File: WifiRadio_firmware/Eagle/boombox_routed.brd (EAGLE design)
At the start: 60.6 x 45.7 mm, 16 parts, among them Y1 16 MHz

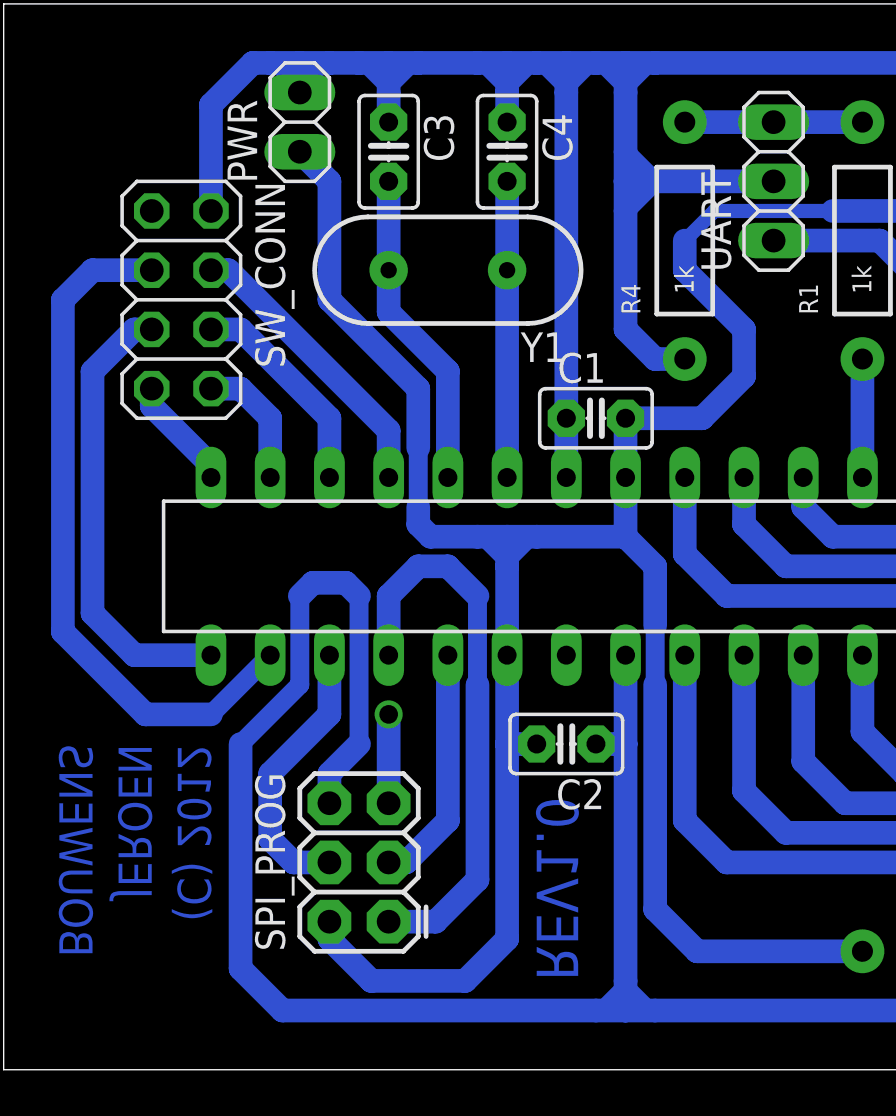
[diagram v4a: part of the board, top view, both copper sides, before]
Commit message: More angle changes
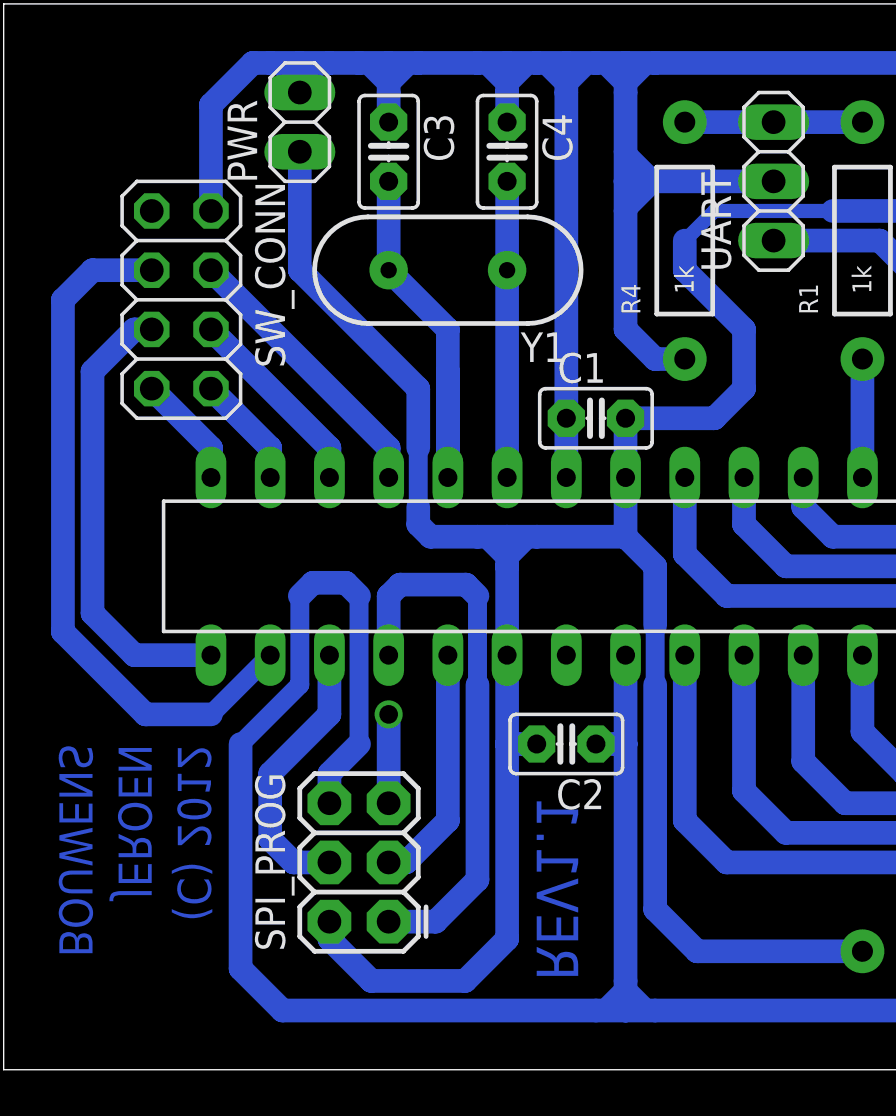
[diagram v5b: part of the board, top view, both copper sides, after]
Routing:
- net N$1: track 13.8 -> 18.3 mm
- net N$23: track 5.61 -> 4.86 mm
- net N$22: track 9.20 -> 8.45 mm
- net N$17: track 24.1 -> 23.5 mm
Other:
- board text added: "REV1.1"
- board text removed: "REV1.0"
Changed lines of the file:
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@@
 <layer number="23" name="tOrigins" color="15" fill="1" visible="yes" active="yes"/>
 <layer number="24" name="bOrigins" color="15" fill="1" visible="yes" active="yes"/>
-<layer number="25" name="tNames" color="7" fill="1" visible="no" active="yes"/>
-<layer number="26" name="bNames" color="7" fill="1" visible="no" active="yes"/>
+<layer number="25" name="tNames" color="7" fill="1" visible="yes" active="yes"/>
+<layer number="26" name="bNames" color="7" fill="1" visible="yes" active="yes"/>
 <layer number="27" name="tValues" color="7" fill="1" visible="no" active="yes"/>
 <layer number="28" name="bValues" color="7" fill="1" visible="no" active="yes"/>
@@
 <text x="8.89" y="15.24" size="1.4224" layer="16" ratio="25" rot="MR270">JEROEN</text>
 <text x="6.35" y="15.24" size="1.4224" layer="16" ratio="25" rot="MR270">BOUWENS</text>
-<text x="25.4" y="5.08" size="1.778" layer="16" ratio="23" rot="MR90">REV1.0</text>
+<text x="25.4" y="5.08" size="1.778" layer="16" ratio="23" rot="MR90">REV1.1</text>
 </plain>
 <attributes>
@@
 <wire x1="24.13" y1="6.87605" x2="22.33395" y2="5.08" width="1.016" layer="16"/>
 <wire x1="22.33395" y1="5.08" x2="18.30605" y2="5.08" width="1.016" layer="16"/>
-<wire x1="31.75" y1="36.83" x2="31.75" y2="35.56" width="1.016" layer="16"/>
-<wire x1="31.75" y1="35.56" x2="34.29" y2="33.02" width="1.016" layer="16"/>
-<wire x1="34.29" y1="33.02" x2="34.29" y2="31.00605" width="1.016" layer="16"/>
-<wire x1="34.29" y1="31.00605" x2="32.49395" y2="29.21" width="1.016" layer="16"/>
-<wire x1="32.49395" y1="29.21" x2="29.21" y2="29.21" width="1.016" layer="16"/>
 <wire x1="48.26" y1="35.56" x2="43.92395" y2="35.56" width="1.016" layer="16"/>
 <wire x1="43.92395" y1="35.56" x2="41.38395" y2="38.1" width="1.016" layer="16"/>
@@
 <wire x1="20.84605" y1="24.13" x2="20.32" y2="24.65605" width="1.016" layer="16"/>
 <wire x1="20.32" y1="24.65605" x2="20.32" y2="25.4" width="1.016" layer="16"/>
-<wire x1="15.24" y1="40.64" x2="16.51" y2="39.37" width="1.016" layer="16"/>
-<wire x1="16.51" y1="39.37" x2="16.51" y2="34.29" width="1.016" layer="16"/>
+<wire x1="15.24" y1="40.64" x2="15.24" y2="35.56" width="1.016" layer="16"/>
 <wire x1="20.32" y1="27.94" x2="20.32" y2="25.4" width="0.8128" layer="16"/>
 <wire x1="24.13" y1="19.05" x2="24.13" y2="22.86" width="1.016" layer="16"/>
@@
 <wire x1="32.27605" y1="6.35" x2="30.48" y2="8.14605" width="1.016" layer="16"/>
 <wire x1="30.48" y1="8.14605" x2="30.48" y2="17.78" width="1.016" layer="16"/>
-<wire x1="16.51" y1="34.29" x2="20.32" y2="30.48" width="1.016" layer="16"/>
+<wire x1="15.24" y1="35.56" x2="20.32" y2="30.48" width="1.016" layer="16"/>
 <wire x1="20.32" y1="30.48" x2="20.32" y2="27.94" width="1.016" layer="16"/>
 <wire x1="24.13" y1="22.86" x2="25.4" y2="24.13" width="0.4064" layer="16"/>
@@
 <wire x1="58.42" y1="35.56" x2="59.69" y2="34.29" width="1.016" layer="16"/>
 <wire x1="59.69" y1="34.29" x2="59.69" y2="36.83" width="1.016" layer="16"/>
-<wire x1="46.99" y1="19.05" x2="46.99" y2="17.78" width="0" layer="19" extent="16-16"/>
 <wire x1="46.99" y1="19.05" x2="46.99" y2="17.78" width="1.016" layer="16"/>
+<wire x1="29.21" y1="29.21" x2="33.02" y2="29.21" width="1.016" layer="16"/>
+<wire x1="33.02" y1="29.21" x2="34.29" y2="30.48" width="1.016" layer="16"/>
+<wire x1="34.29" y1="30.48" x2="34.29" y2="33.02" width="1.016" layer="16"/>
+<wire x1="34.29" y1="33.02" x2="31.75" y2="35.56" width="1.016" layer="16"/>
+<wire x1="31.75" y1="35.56" x2="31.75" y2="36.83" width="1.016" layer="16"/>
 </signal>
 <signal name="GND">
@@
 <contactref element="C3" pad="2"/>
 <contactref element="ATMEGA328" pad="10"/>
-<wire x1="19.05" y1="39.37" x2="19.05" y2="35.56" width="1.016" layer="16"/>
 <wire x1="21.59" y1="26.67" x2="21.59" y2="31.22395" width="1.016" layer="16"/>
-<wire x1="21.59" y1="31.22395" x2="19.05" y2="33.76395" width="1.016" layer="16"/>
-<wire x1="19.05" y1="33.76395" x2="19.05" y2="35.56" width="1.016" layer="16"/>
+<wire x1="21.59" y1="26.67" x2="21.59" y2="33.02" width="1.016" layer="16"/>
+<wire x1="21.59" y1="33.02" x2="19.05" y2="35.56" width="1.016" layer="16"/>
+<wire x1="19.05" y1="35.56" x2="19.05" y2="39.37" width="1.016" layer="16"/>
 </signal>
 <signal name="N$2">
@@
 <contactref element="SPI_PROG" pad="1"/>
 <wire x1="19.05" y1="19.05" x2="19.05" y2="21.59" width="1.016" layer="16"/>
-<wire x1="19.05" y1="21.59" x2="20.32" y2="22.86" width="1.016" layer="16"/>
-<wire x1="20.32" y1="22.86" x2="21.59" y2="22.86" width="1.016" layer="16"/>
-<wire x1="21.59" y1="22.86" x2="22.86" y2="21.59" width="1.016" layer="16"/>
+<wire x1="19.05" y1="21.59" x2="19.5351" y2="22.0751" width="1.016" layer="16"/>
+<wire x1="19.5351" y1="22.0751" x2="22.3749" y2="22.0751" width="1.016" layer="16"/>
+<wire x1="22.3749" y1="22.0751" x2="22.86" y2="21.59" width="1.016" layer="16"/>
 <wire x1="22.86" y1="21.59" x2="22.86" y2="17.78" width="0.8128" layer="16"/>
 <wire x1="19.05" y1="7.62" x2="21.06395" y2="7.62" width="1.016" layer="16"/>
@@
 <signal name="N$24">
 <contactref element="ATMEGA328" pad="11"/>
-<wire x1="19.05" y1="26.67" x2="19.05" y2="28.68395" width="1.016" layer="16"/>
-<wire x1="19.05" y1="28.68395" x2="12.17395" y2="35.56" width="1.016" layer="16"/>
-<wire x1="12.17395" y1="35.56" x2="11.43" y2="35.56" width="1.016" layer="16"/>
 <contactref element="SW_CONN" pad="4"/>
+<wire x1="11.43" y1="35.56" x2="19.05" y2="27.94" width="1.016" layer="16"/>
+<wire x1="19.05" y1="27.94" x2="19.05" y2="26.67" width="1.016" layer="16"/>
 </signal>
 <signal name="N$23">
 <contactref element="SW_CONN" pad="8"/>
 <contactref element="ATMEGA328" pad="13"/>
-<wire x1="13.97" y1="26.67" x2="13.97" y2="29.21" width="1.016" layer="16"/>
-<wire x1="13.97" y1="29.21" x2="12.7" y2="30.48" width="1.016" layer="16"/>
-<wire x1="12.7" y1="30.48" x2="11.43" y2="30.48" width="1.016" layer="16"/>
+<wire x1="13.97" y1="26.67" x2="13.97" y2="27.94" width="1.016" layer="16"/>
+<wire x1="13.97" y1="27.94" x2="11.43" y2="30.48" width="1.016" layer="16"/>
 </signal>
 <signal name="N$11">
@@
 <contactref element="SW_CONN" pad="7"/>
 <contactref element="ATMEGA328" pad="14"/>
-<wire x1="11.43" y1="26.67" x2="11.43" y2="27.19605" width="1.016" layer="16"/>
-<wire x1="11.43" y1="27.19605" x2="8.89" y2="29.73605" width="1.016" layer="16"/>
-<wire x1="8.89" y1="29.73605" x2="8.89" y2="30.48" width="1.016" layer="16"/>
+<wire x1="8.89" y1="30.48" x2="11.43" y2="27.94" width="1.016" layer="16"/>
+<wire x1="11.43" y1="27.94" x2="11.43" y2="26.67" width="1.016" layer="16"/>
 </signal>
 <signal name="N$22">
 <contactref element="SW_CONN" pad="6"/>
 <contactref element="ATMEGA328" pad="12"/>
-<wire x1="16.51" y1="26.67" x2="16.51" y2="29.21" width="1.016" layer="16"/>
-<wire x1="16.51" y1="29.21" x2="12.7" y2="33.02" width="1.016" layer="16"/>
-<wire x1="12.7" y1="33.02" x2="11.43" y2="33.02" width="1.016" layer="16"/>
+<wire x1="16.51" y1="26.67" x2="16.51" y2="27.94" width="1.016" layer="16"/>
+<wire x1="16.51" y1="27.94" x2="11.43" y2="33.02" width="1.016" layer="16"/>
 </signal>
 <signal name="N$21">

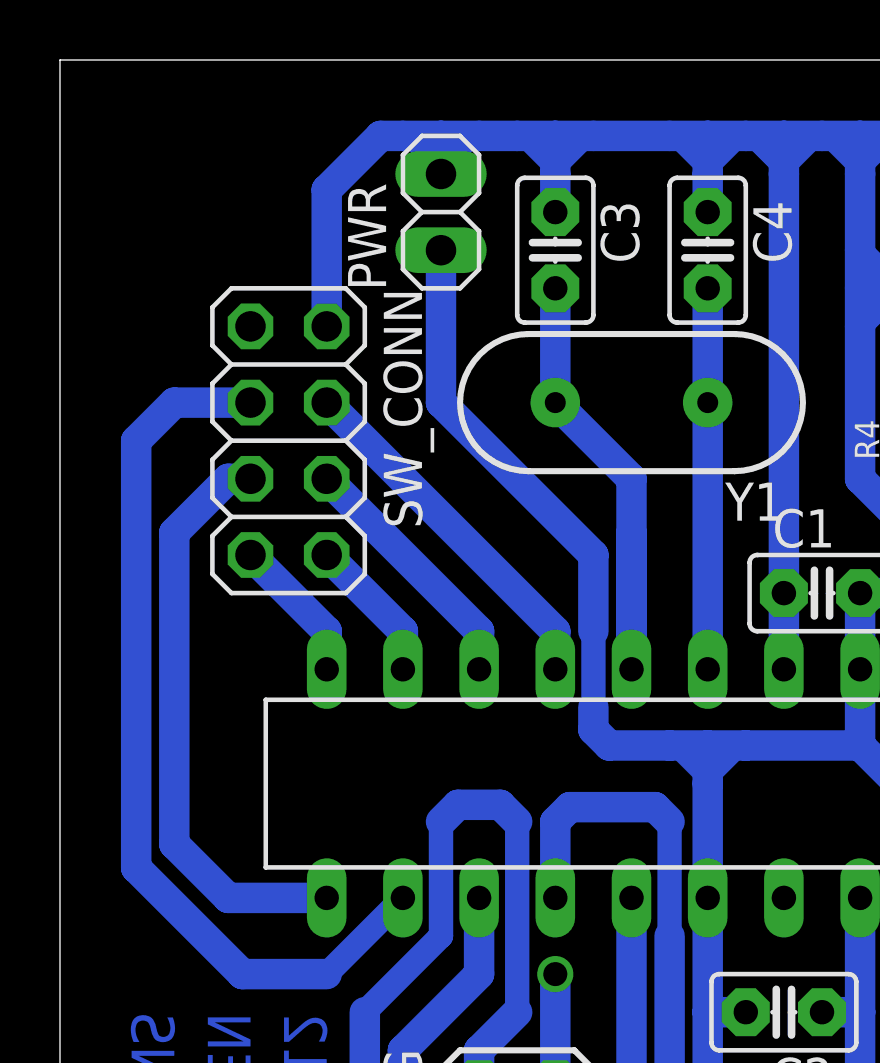
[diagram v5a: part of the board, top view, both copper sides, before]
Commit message: Added back the 10 uF stabilizing cap
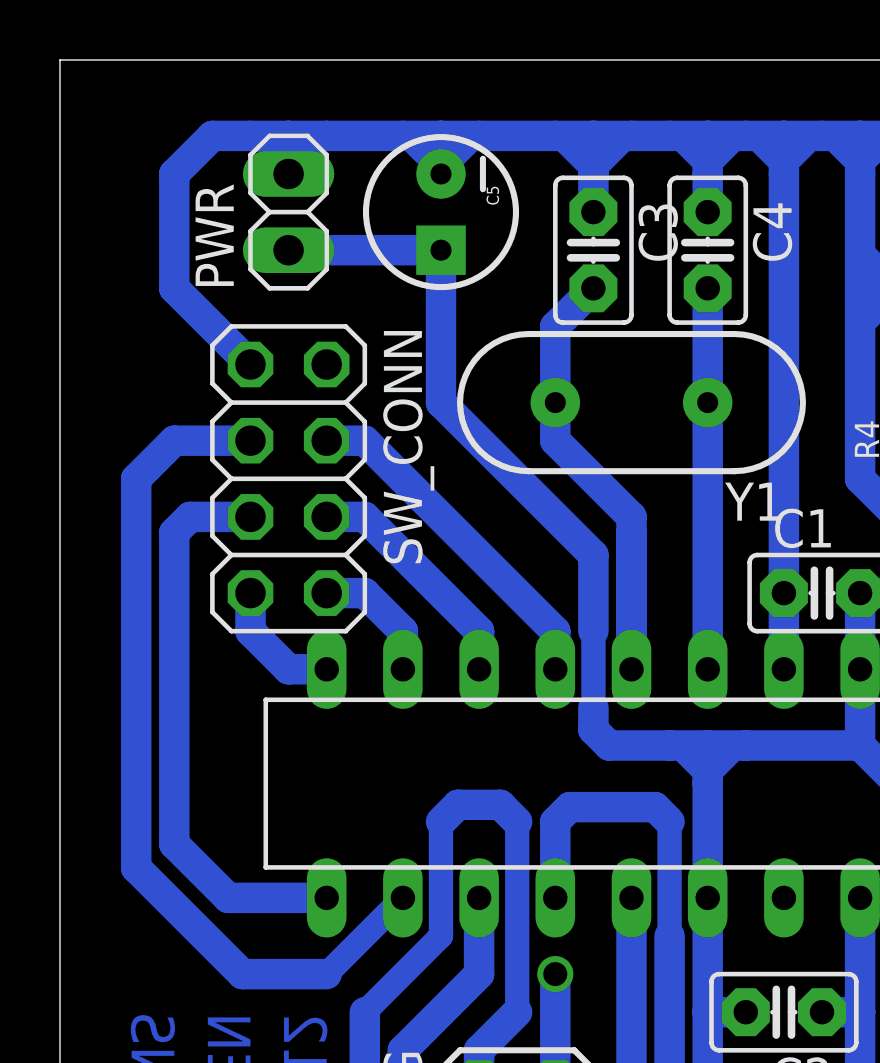
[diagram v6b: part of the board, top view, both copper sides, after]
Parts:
- added C5: 10uF, SparkFun:CPOL-RADIAL-10UF-25V
- moved PWR 5.08 mm to (10.2, 41.9)
- moved C3 1.27 mm to (20.3, 40.6)
- moved SW_CONN 1.27 mm to (10.2, 33.0)
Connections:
- net GND: now also C5.2, SW_CONN.1; no longer SW_CONN.2
- net VCC: now also C5.1
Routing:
- net GND: track 310.3 -> 317.8 mm
- net VCC: track 172.2 -> 177.2 mm
- net N$25: track 30.0 -> 28.7 mm
- net N$24: track 12.0 -> 11.5 mm
- net N$22: track 8.45 -> 7.93 mm
- net N$21: track 19.5 -> 19.0 mm
- net N$23: track 4.86 -> 4.34 mm
- net N$19: track 4.86 -> 4.34 mm
- net N$1: track 18.3 -> 18.8 mm

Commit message: Modified boards, changed pin asignment in lcd driver
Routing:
- net N$27: track 8.89 -> 61.6 mm
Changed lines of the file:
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@@
 <grid distance="0.05" unitdist="inch" unit="inch" style="lines" multiple="1" display="no" altdistance="0.025" altunitdist="inch" altunit="inch"/>
 <layers>
-<layer number="1" name="Top" color="4" fill="1" visible="no" active="yes"/>
+<layer number="1" name="Top" color="4" fill="1" visible="yes" active="yes"/>
 <layer number="16" name="Bottom" color="1" fill="1" visible="yes" active="yes"/>
 <layer number="17" name="Pads" color="2" fill="1" visible="yes" active="yes"/>
 <layer number="18" name="Vias" color="2" fill="1" visible="yes" active="yes"/>
-<layer number="19" name="Unrouted" color="6" fill="1" visible="no" active="yes"/>
-<layer number="20" name="Dimension" color="15" fill="1" visible="no" active="yes"/>
-<layer number="21" name="tPlace" color="15" fill="1" visible="no" active="yes"/>
-<layer number="22" name="bPlace" color="7" fill="1" visible="no" active="yes"/>
-<layer number="23" name="tOrigins" color="15" fill="1" visible="no" active="yes"/>
-<layer number="24" name="bOrigins" color="15" fill="1" visible="no" active="yes"/>
-<layer number="25" name="tNames" color="7" fill="1" visible="no" active="yes"/>
-<layer number="26" name="bNames" color="7" fill="1" visible="no" active="yes"/>
+<layer number="19" name="Unrouted" color="6" fill="1" visible="yes" active="yes"/>
+<layer number="20" name="Dimension" color="15" fill="1" visible="yes" active="yes"/>
+<layer number="21" name="tPlace" color="15" fill="1" visible="yes" active="yes"/>
+<layer number="22" name="bPlace" color="7" fill="1" visible="yes" active="yes"/>
+<layer number="23" name="tOrigins" color="15" fill="1" visible="yes" active="yes"/>
+<layer number="24" name="bOrigins" color="15" fill="1" visible="yes" active="yes"/>
+<layer number="25" name="tNames" color="7" fill="1" visible="yes" active="yes"/>
+<layer number="26" name="bNames" color="7" fill="1" visible="yes" active="yes"/>
 <layer number="27" name="tValues" color="7" fill="1" visible="no" active="yes"/>
 <layer number="28" name="bValues" color="7" fill="1" visible="no" active="yes"/>
@@
 <wire x1="44.45" y1="26.67" x2="44.45" y2="31.75" width="1.016" layer="16"/>
 <wire x1="19.05" y1="16.51" x2="19.05" y2="12.7" width="1.016" layer="16"/>
-<wire x1="19.05" y1="16.51" x2="44.45" y2="26.67" width="0" layer="19" extent="1-1"/>
+<wire x1="19.05" y1="16.51" x2="10.68605" y2="16.51" width="1.016" layer="1"/>
+<wire x1="10.68605" y1="16.51" x2="8.89" y2="18.30605" width="1.016" layer="1"/>
+<wire x1="8.89" y1="18.30605" x2="8.89" y2="21.06395" width="1.016" layer="1"/>
+<wire x1="8.89" y1="21.06395" x2="10.68605" y2="22.86" width="1.016" layer="1"/>
+<wire x1="10.68605" y1="22.86" x2="42.65395" y2="22.86" width="1.016" layer="1"/>
+<wire x1="42.65395" y1="22.86" x2="44.45" y2="24.65605" width="1.016" layer="1"/>
+<wire x1="44.45" y1="24.65605" x2="44.45" y2="26.67" width="1.016" layer="1"/>
 </signal>
 <signal name="N$30">
